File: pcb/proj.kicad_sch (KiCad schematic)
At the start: 125 parts, among them J1 Conn_02x05_Odd_Even, SW1 Reset, SW10 8, SW11 9, SW12 /, SW13 Deg/Rad, SW14 Clear, SW15 4, SW16 5, SW17 6, SW18 X, SW19 Constants, SW2 Y/Stats, SW20 Del, SW21 1, SW22 2, SW23 3, SW24 -, SW25 Alpha, SW26 (/), SW27 Sin(x)/Sin-1(x), SW28 Cos(x)/Cos-1(x), SW29 Tan(x)/Tan-1(x), SW3 ./,, SW30 +, SW31 2nd, SW32 Γ(x), SW33 x^y/y√x, SW34 x^2/√x, SW35 log(x)/ln(x), SW36 e^x/10^x, SW37 Graph, SW38 Programs, SW39 Left, SW4 0, SW40 Up, SW41 Right, SW42 Down, SW43 Power, SW44 FPU BOOT0, SW45 Reset, SW5 +/-, SW6 Solve/=, SW7 Sci/Norm, SW8 X/Matrix, SW9 7, U1 PIC16C74, U2 STM32F401RCTx, U3 74HC238, U4 ISL9111EH50Z-T7A, U5 SN74LVC1G32DBVR, Y1 20MHz

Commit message: v 1.2
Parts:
- removed B2: 2032, Parts:BAT_BAT-HLD-001-THM, symbol Device:Battery_Cell
- B1: value 2032 -> 2x AA; footprint Parts:BAT_BAT-HLD-001-THM -> Battery:BatteryHolder_MPD_BC2AAPC_2xAA
- C1, C2: footprint Capacitor_SMD:C_0402_1005Metric_Pad0.74x0.62mm_HandSolder -> Capacitor_SMD:C_1206_3216Metric_Pad1.33x1.80mm_HandSolder
- D1, D10, D11, D12, D13, D14, D15, D16, D17, D18, D19, D2, D20, D21, D22, D23, D24, D25, D26, D27, D28, D29, D3, D30, D31, D32, D33, D34, D35, D36, D37, D38, D39, D4, D40, D41, D42, D5, D6, D7, D8, D9: value BAS7002 -> S040S2R0; footprint Diode_SMD:D_SOD-523 -> Diode_SMD:D_1206_3216Metric_Pad1.42x1.75mm_HandSolder

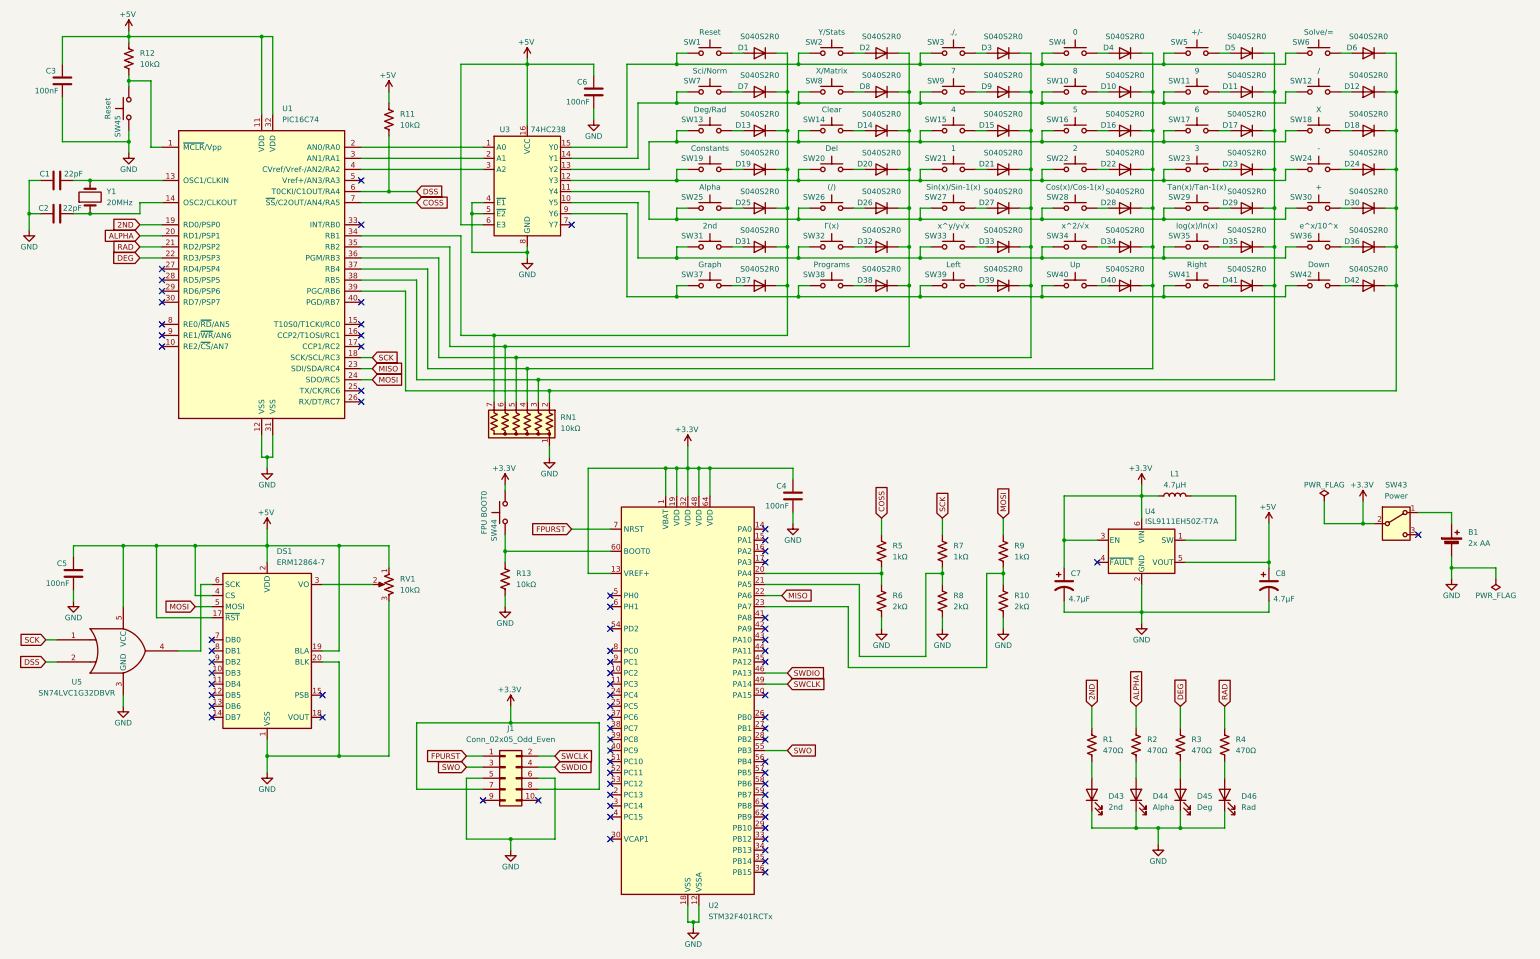
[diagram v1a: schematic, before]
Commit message: update schematics + add CO RDY trace
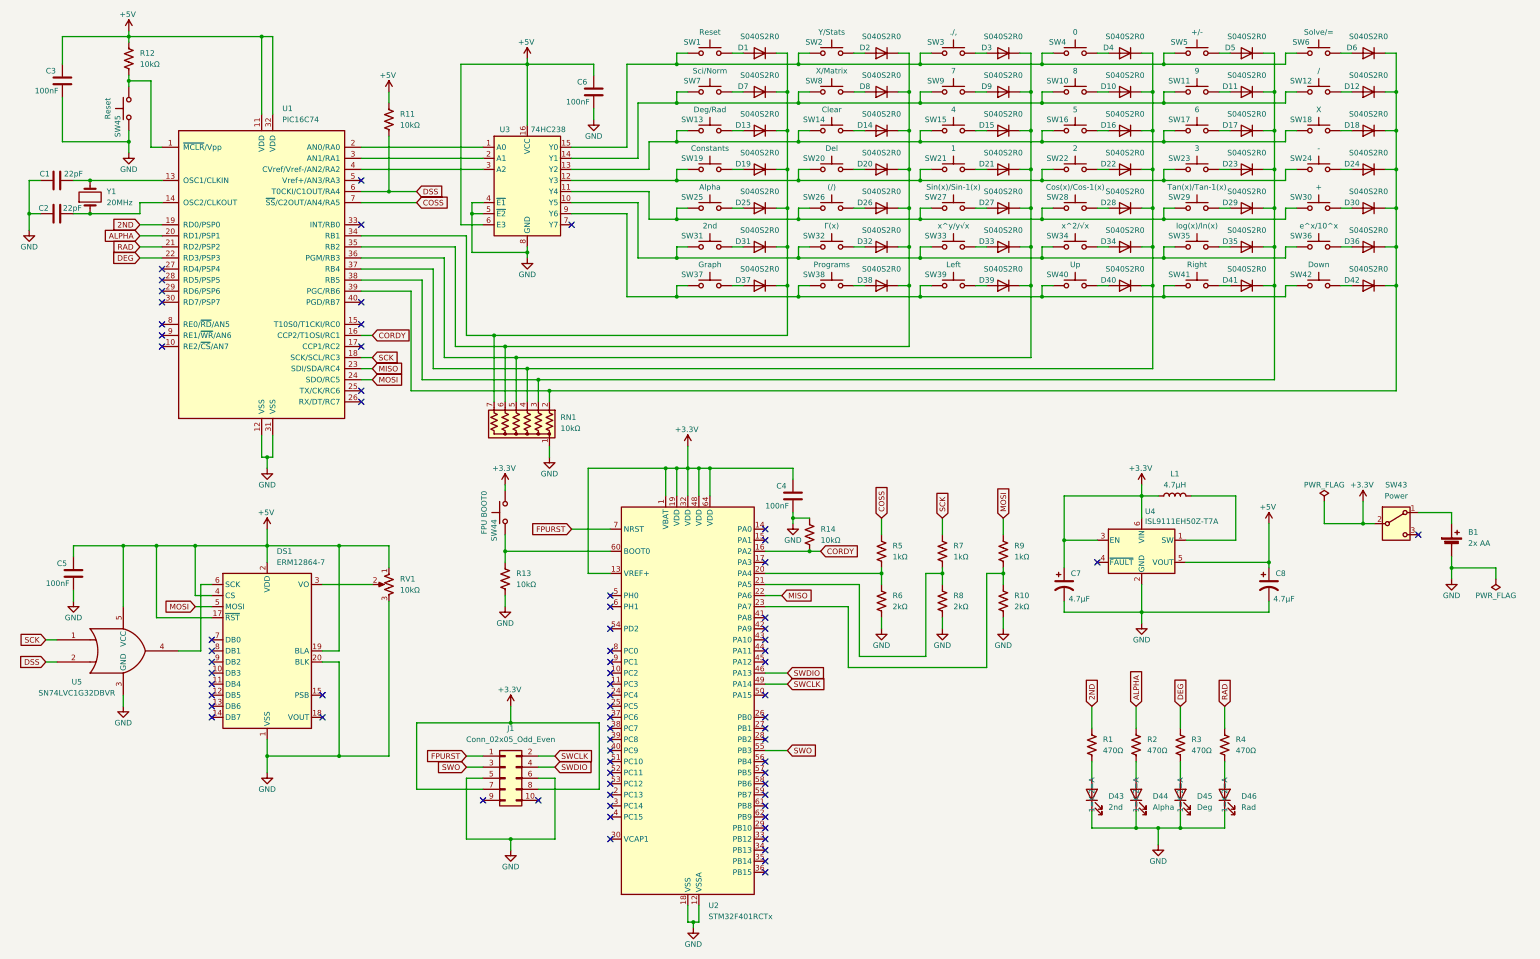
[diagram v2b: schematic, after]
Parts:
- added R14: 10kΩ, Resistor_SMD:R_1206_3216Metric_Pad1.30x1.75mm_HandSolder, symbol Device:R_US
- U4: footprint Package_TO_SOT_SMD:SOT-23-6_Handsoldering -> Package_TO_SOT_SMD:SOT-363_SC-70-6
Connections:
- net GND: now also R14.1
- net CORDY: now reaches U1.16 (CCP2/T1OSI/RC1)
- net CORDY: now also U2.16 (PA2), R14.2
- no-connect marks 74 -> 72

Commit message: add buzzer and join resets
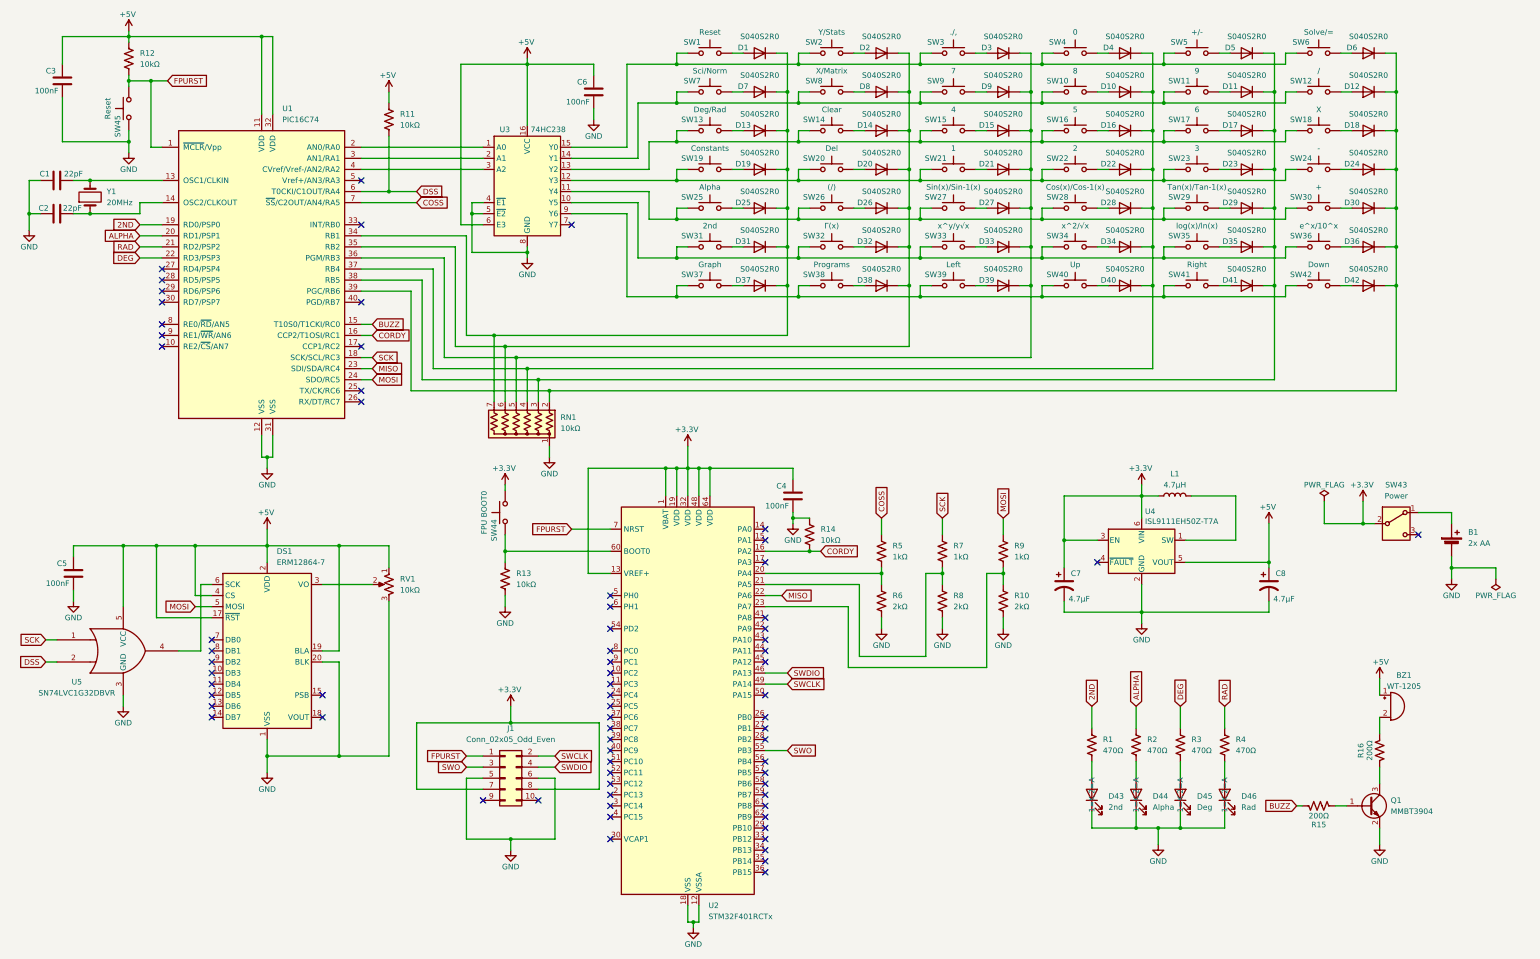
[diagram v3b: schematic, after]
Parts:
- added BZ1: WT-1205, Buzzer_Beeper:Buzzer_TDK_PS1240P02BT_D12.2mm_H6.5mm, symbol Device:Buzzer
- added Q1: MMBT3904, Package_TO_SOT_SMD:SOT-23, symbol Transistor_BJT:MMBT3904
- added R15, R16: 200Ω, Resistor_SMD:R_1206_3216Metric_Pad1.30x1.75mm_HandSolder, symbol Device:R_US
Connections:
- net +5V: now also BZ1.1 (+)
- net FPURST: now also R12.2, SW45.2, U1.1 (~{MCLR}/Vpp)
- net GND: now also Q1.2 (E)
- net BUZZ: now reaches U1.15 (T10S0/T1CKI/RC0)
- net BUZZ: now also R15.2
- new net: Q1.1 (B), R15.1
- new net: Q1.3 (C), R16.1
- new net: BZ1.2 (-), R16.2
- no-connect marks 72 -> 71

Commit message: fix
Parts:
- removed R16: 200Ω, Resistor_SMD:R_1206_3216Metric_Pad1.30x1.75mm_HandSolder, symbol Device:R_US
- BZ1: footprint Buzzer_Beeper:Buzzer_TDK_PS1240P02BT_D12.2mm_H6.5mm -> Buzzer_Beeper:Buzzer_12x9.5RM7.6
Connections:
- net at Q1.3 (C): now also BZ1.2 (-)
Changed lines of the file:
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@@
 	(wire
 		(pts
-			(xy 326.39 175.26) (xy 326.39 179.07)
-		)
-		(stroke
-			(width 0)
-			(type default)
-		)
-	)
-	(wire
-		(pts
 			(xy 193.04 31.75) (xy 193.04 34.29)
 		)
@@
 	(wire
 		(pts
-			(xy 326.39 186.69) (xy 326.39 190.5)
-		)
-		(stroke
-			(width 0)
-			(type default)
-		)
-	)
-	(wire
-		(pts
 			(xy 299.72 22.86) (xy 302.26 22.86)
 		)
@@
 	(wire
 		(pts
+			(xy 326.39 175.26) (xy 326.39 190.5)
+		)
+		(stroke
+			(width 0)
+			(type default)
+		)
+	)
+	(wire
+		(pts
 			(xy 220.98 49.53) (xy 220.98 52.07)
 		)
@@
 			)
 		)
-		(property "Footprint" "Buzzer_Beeper:Buzzer_TDK_PS1240P02BT_D12.2mm_H6.5mm"
+		(property "Footprint" "Buzzer_Beeper:Buzzer_12x9.5RM7.6"
 			(at 328.295 170.18 90)
 			(effects
@@
 					(unit 1)
 				)
-			)
-		)
-	)
-	(symbol
-		(lib_id "Device:R_US")
-		(at 326.39 182.88 0)
-		(mirror x)
-		(unit 1)
-		(exclude_from_sim no)
-		(in_bom yes)
-		(on_board yes)
-		(dnp no)
-		(property "Reference" "R16"
-			(at 322.072 182.88 90)
-			(effects
-				(font
-					(size 1.27 1.27)
-				)
-			)
-		)
-		(property "Value" "200Ω"
-			(at 324.104 182.88 90)
-			(effects
-				(font
-					(size 1.27 1.27)
-				)
-			)
-		)
-		(property "Footprint" "Resistor_SMD:R_1206_3216Metric_Pad1.30x1.75mm_HandSolder"
-			(at 327.406 182.626 90)
-			(effects
-				(font
-					(size 1.27 1.27)
-				)
-				(hide yes)
-			)
-		)
-		(property "Datasheet" "~"
-			(at 326.39 182.88 0)
-			(effects
-				(font
-					(size 1.27 1.27)
-				)
-				(hide yes)
-			)
-		)
-		(property "Description" "Resistor, US symbol"
-			(at 326.39 182.88 0)
-			(effects
-				(font
-					(size 1.27 1.27)
-				)
-				(hide yes)
-			)
-		)
-		(pin "1"
-		)
-		(pin "2"
-		)
-		(instances
-			(project "proj"
-				(path "/9b3fd51f-0cc8-4d93-a874-8128b084ae71"
-					(reference "R16")
-					(unit 1)
-				)

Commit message: fix
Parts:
- U4: footprint Package_TO_SOT_SMD:SOT-363_SC-70-6 -> Package_TO_SOT_SMD:SOT-23-6_Handsoldering
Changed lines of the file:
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@@
 			)
 		)
-		(property "Footprint" "Package_TO_SOT_SMD:SOT-363_SC-70-6"
+		(property "Footprint" "Package_TO_SOT_SMD:SOT-23-6_Handsoldering"
 			(at 273.05 143.51 0)
 			(effects

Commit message: add titles
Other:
- title: (none) -> PICalculator
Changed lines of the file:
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@@
 	(generator_version "9.0")
 	(paper "A3")
+	(title_block
+		(title "PICalculator")
+		(date "2025-06-01")
+		(rev "1.2")
+	)
 	(junction
 		(at 246.38 49.53)

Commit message: w
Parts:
- removed R12: 10kΩ, Resistor_SMD:R_1206_3216Metric_Pad1.30x1.75mm_HandSolder, symbol Device:R_US
- added C10: 100nF, Capacitor_SMD:C_1206_3216Metric_Pad1.33x1.80mm_HandSolder, symbol Device:C
- added C9: 2.2μF, Capacitor_SMD:C_1206_3216Metric_Pad1.33x1.80mm_HandSolder, symbol Device:C
- added U8: SN74LV1T34DBV, Package_TO_SOT_SMD:SOT-23-5, symbol Logic_LevelTranslator:SN74LV1T34DBV
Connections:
- net +5V: now also C10.1, U8.5 (VCC)
- net FPURST: now also U8.2 (A); no longer U1.1 (~{MCLR}/Vpp)
- net GND: now also C10.2, C9.2, U8.3 (GND)
- net at U2.30 (VCAP1): now also C9.1
- new net: U1.1 (~{MCLR}/Vpp), U8.4 (Y)
- no-connect marks 71 -> 70
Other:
- moved on the sheet: C3, SW45
